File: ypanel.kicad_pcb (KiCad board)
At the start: 6 copper layers, 64 x 58 mm, 58 parts, among them IC2 TSL2561, J1 XF2M-1015-1A, J2 Conn_Coaxial, J3 BATTERY CONNECTOR, J4 B2B-PH-SM4-TB_LF__SN_, U2 Value, U3 SW_SPDT, U4 SW_SPDT

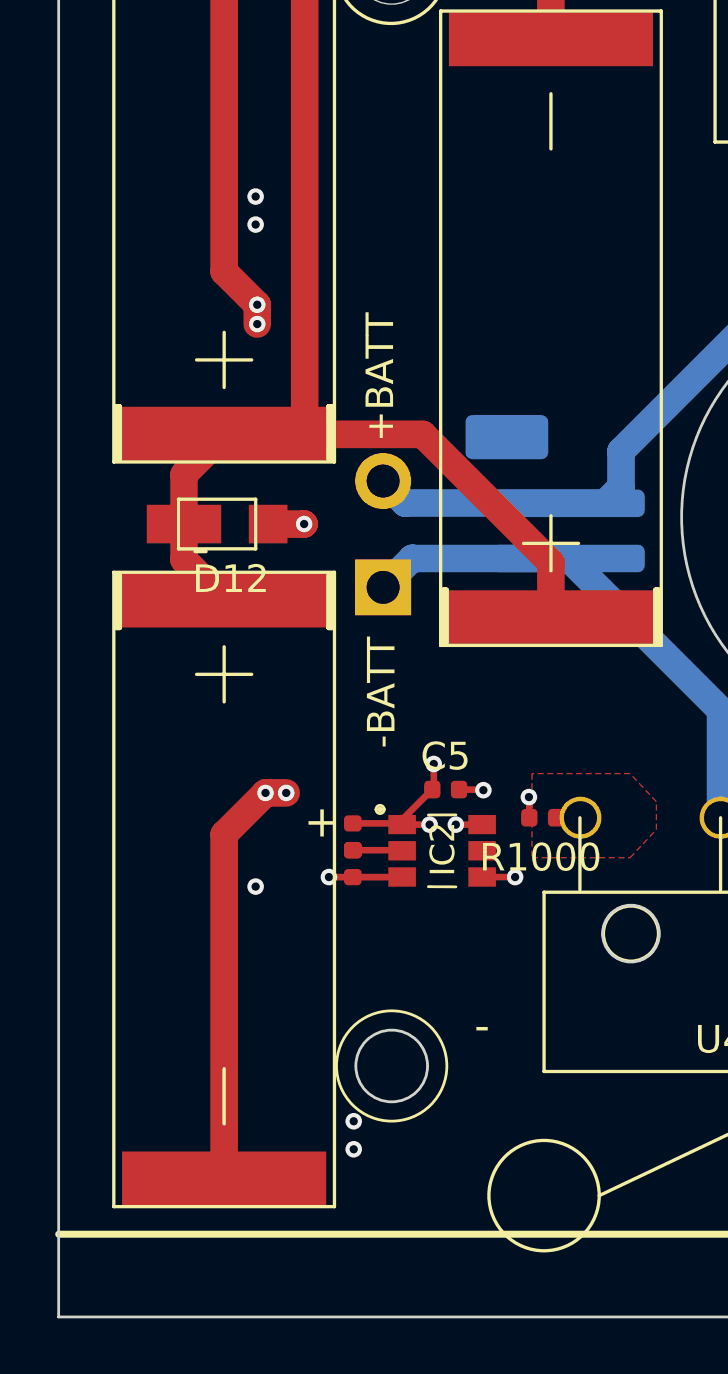
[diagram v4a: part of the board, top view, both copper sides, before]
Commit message: Changed magnetorquer coils
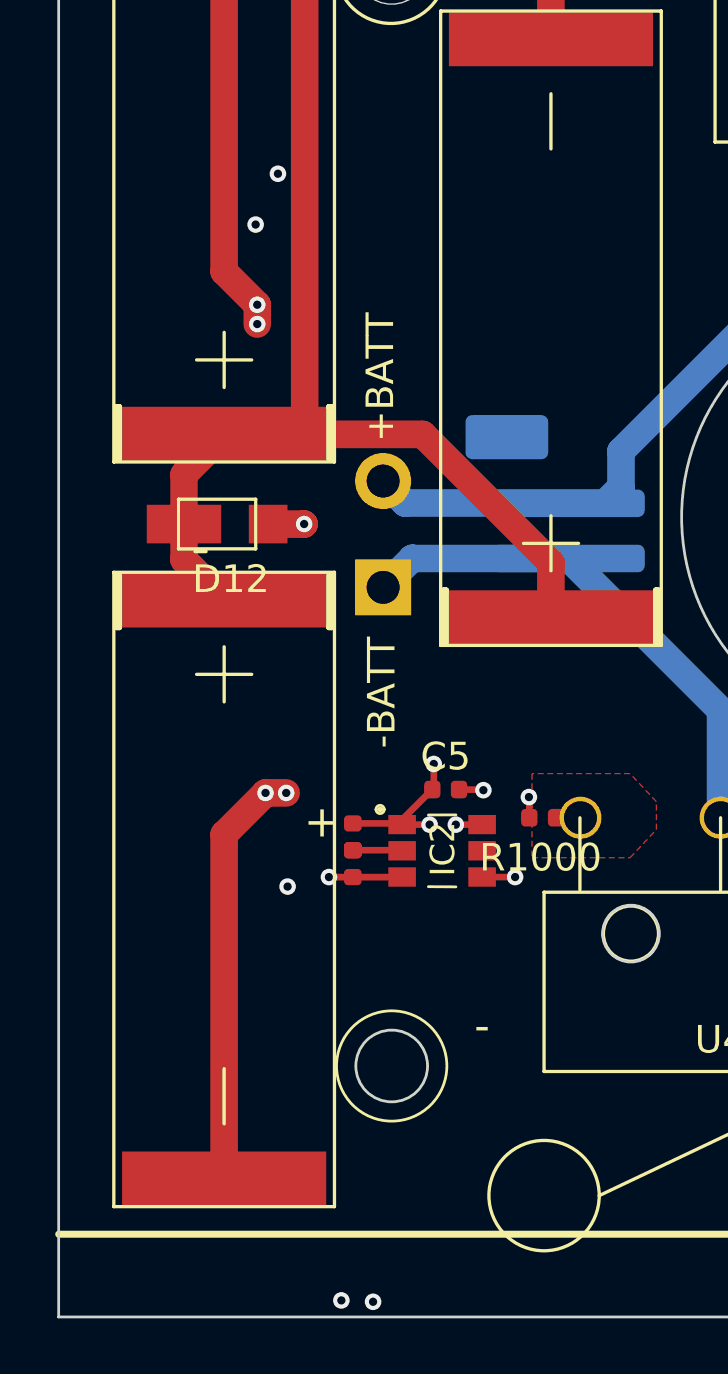
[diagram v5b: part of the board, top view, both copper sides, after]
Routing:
- net /coil: track 15890.0 -> 16804.3 mm
- net COIL_N: track 50.9 -> 43.0 mm
- net BATT_N: track 34.9 -> 30.4 mm
- net COIL_P: track 50.3 -> 45.8 mm
- net BATT_P: track 62.1 -> 58.9 mm

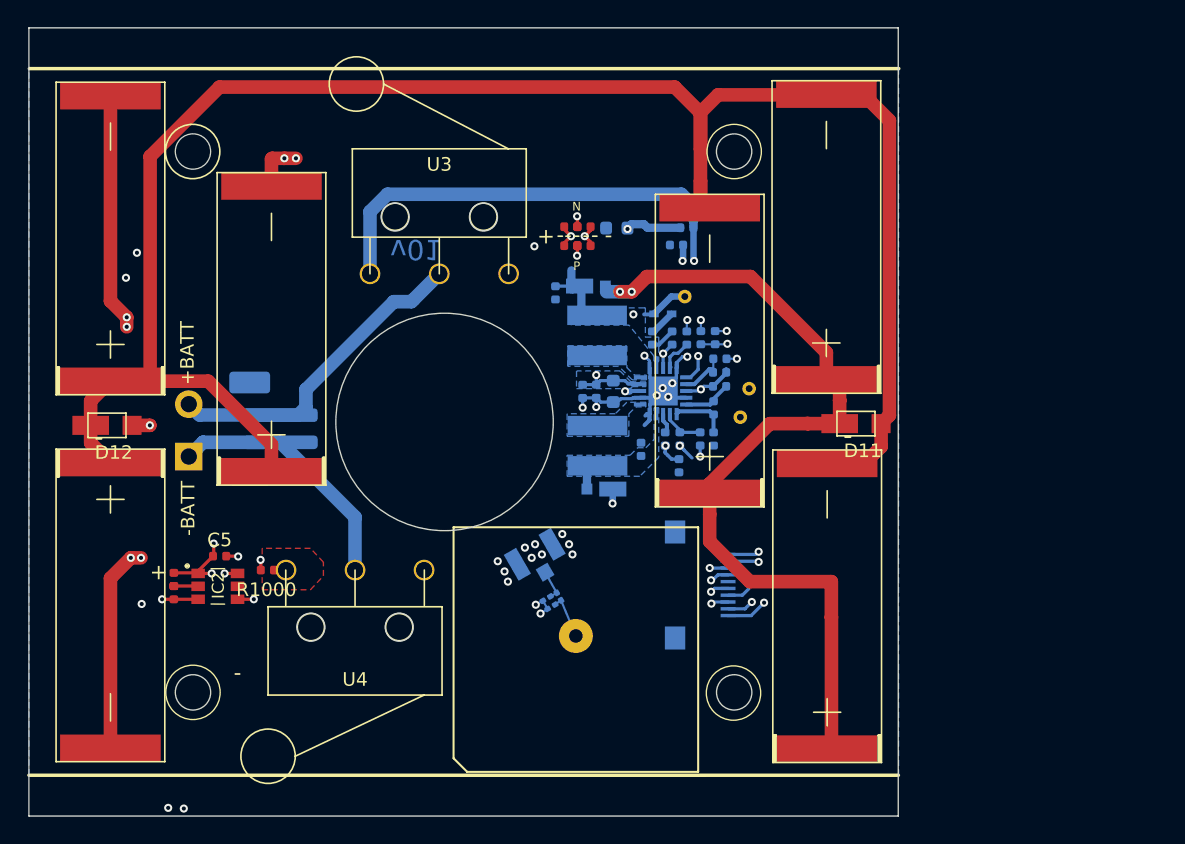
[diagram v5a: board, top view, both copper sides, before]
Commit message: added fiducials, regenerated 3d model and gerbers
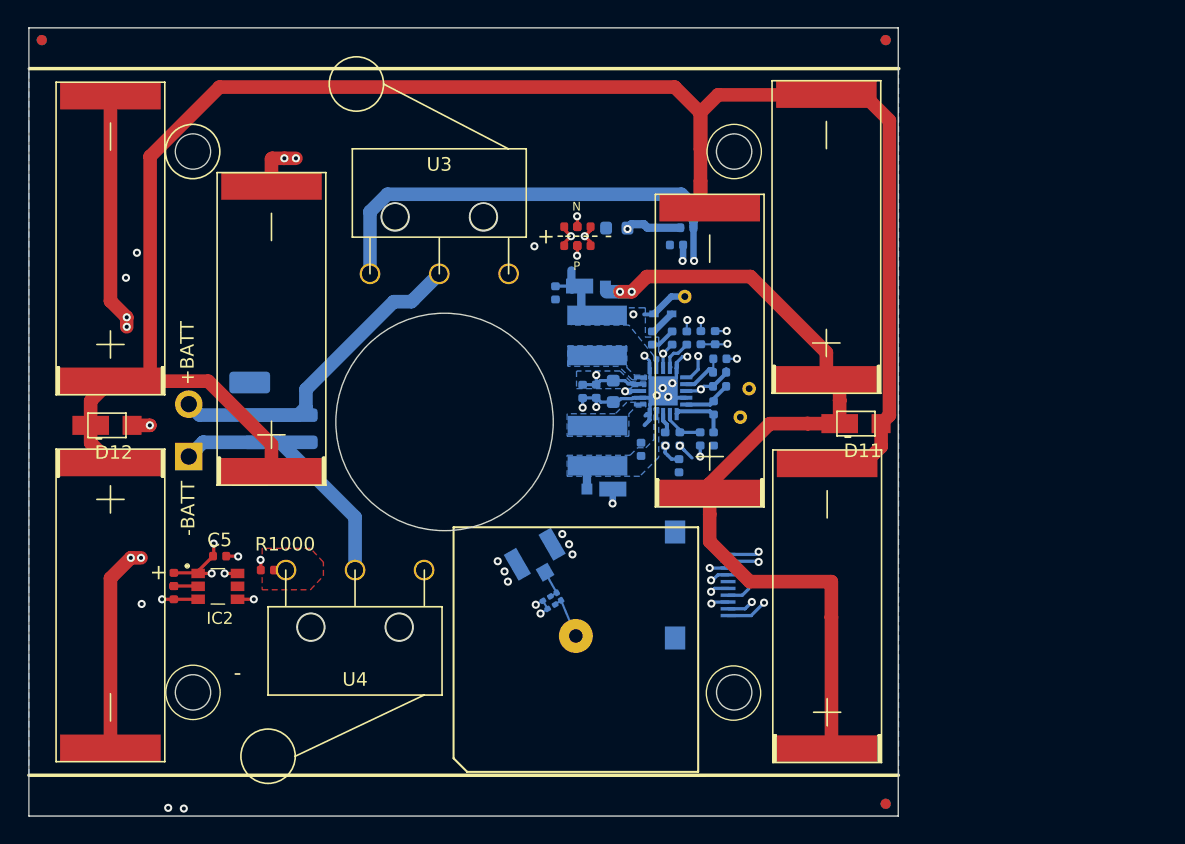
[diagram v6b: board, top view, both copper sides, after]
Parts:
- added REF**: Fiducial_0.75mm_Mask1.5mm, Fiducial:Fiducial_0.75mm_Mask1.5mm, B.Cu at (114.0, 70.9)
- added REF**: Fiducial_0.75mm_Mask1.5mm, Fiducial:Fiducial_0.75mm_Mask1.5mm, B.Cu at (176.1, 70.9)
- added REF**: Fiducial_0.75mm_Mask1.5mm, Fiducial:Fiducial_0.75mm_Mask1.5mm, B.Cu at (176.1, 127.1)
- added REF**: Fiducial_0.75mm_Mask1.5mm, Fiducial:Fiducial_0.75mm_Mask1.5mm, F.Cu at (176.1, 127.1)
- added REF**: Fiducial_0.75mm_Mask1.5mm, Fiducial:Fiducial_0.75mm_Mask1.5mm, F.Cu at (176.1, 70.9)
- added REF**: Fiducial_0.75mm_Mask1.5mm, Fiducial:Fiducial_0.75mm_Mask1.5mm, F.Cu at (114.0, 70.9)
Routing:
- net COIL_P: track 45.8 -> 48.3 mm
- net COIL_N: track 43.0 -> 44.2 mm
- net GND: vias 36 -> 32
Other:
- rule pad_to_mask_clearance: 0.0508 -> 0.049
- rule solder_mask_min_width: 0.25 -> 0.099
- board text added: "v02"

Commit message: clean up & manufacturing output for v3
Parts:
- removed C12, C13: TBD, Capacitor_SMD:C_0201_0603Metric
- removed L3: TBD, Inductor_SMD:L_0201_0603Metric
- moved TP2 36.1 mm to (130.9, 88.1)
- moved REF** 7.15 mm to (174.5, 120.1) (x2)
- moved REF** 7.15 mm to (116.7, 77.5) (x2)
- moved REF** 6.93 mm to (174.0, 77.5) (x2)
- moved R1000 1.70 mm to (130.6, 108.2), turned to 90 degrees
- moved C1 1.33 mm to (159.8, 103.0)
- moved J2 1.00 mm to (149.5, 109.5), turned to 125 degrees
- moved TP1 0.97 mm to (165.0, 99.6)
- moved R5 0.33 mm to (163.4, 98.3)
- moved R8 0.28 mm to (162.1, 100.2)
- moved R12 0.20 mm to (163.7, 92.8)
- moved D2 0.16 mm to (155.3, 104.1)
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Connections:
- IC2 pad 5: (no net) -> Net-(IC2-Pad5)
- J1 pad 5: (no net) -> BURN1
- J2 pad 1: Net-(C12-Pad1) -> Net-(AE1-Pad1)
- U3 pad 1: (no net) -> Net-(U3-Pad1)
- U4 pad 1: (no net) -> Net-(U4-Pad1)
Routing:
- net GND: track 68.8 -> 65.4 mm, vias 32 -> 31
- net Net-(C12-Pad1): track 2.27 -> 0.00 mm
- net Net-(AE1-Pad1): track 3.37 -> 5.39 mm
- net /VSOLAR_FULL: track 65.6 -> 67.1 mm
- net VOUT_EN: track 11.4 -> 10.1 mm
- net +3V3: track 65.1 -> 63.8 mm, vias 4 -> 3
- net Net-(D11-Pad2): track 136.4 -> 135.2 mm
- net Net-(J3-Pad1): track 18.9 -> 19.6 mm
- net Net-(R7-Pad2): track 3.80 -> 3.23 mm
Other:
- board text added: "JLCJLCJLCJLC"
- board text removed: "Cable Pinout 1.BATT_P 2.BATT_N 3.SDA 4.SCL 5.BURN 6.3V3 7.GND 8.GND 9.COIL_N 10.COIL_P"
- board text removed: "coil_n"
- board text removed: "coil_p"
- board text removed: "v01"

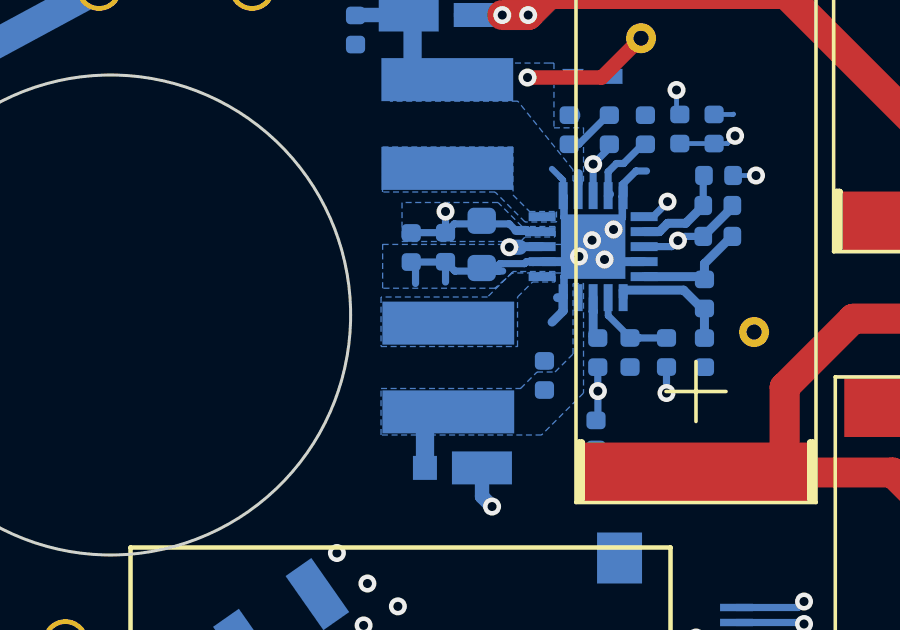
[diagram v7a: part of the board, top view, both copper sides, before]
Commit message: should actually be v3
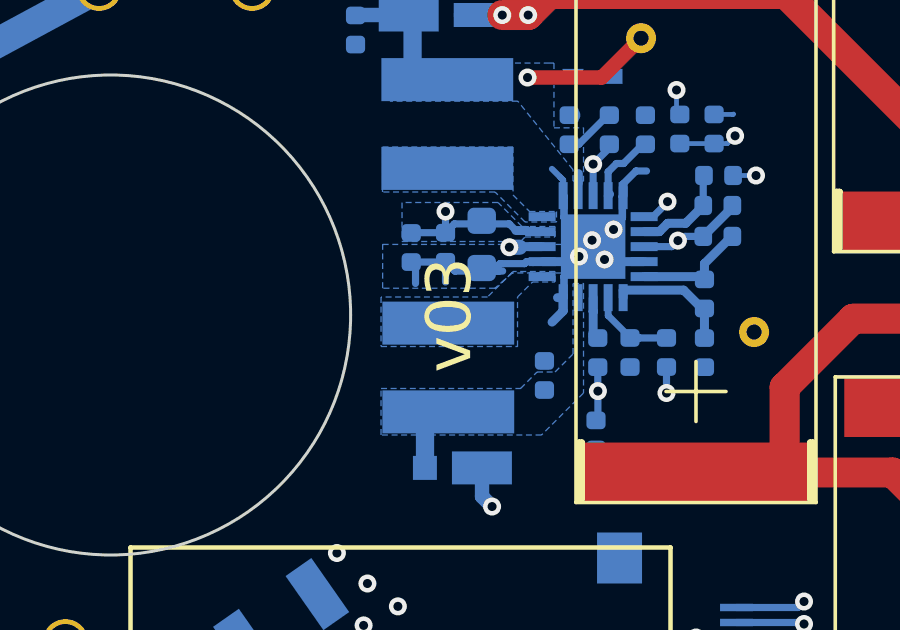
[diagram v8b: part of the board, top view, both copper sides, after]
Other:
- board text added: "v03"
- board text removed: "v02"
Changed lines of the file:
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@@
   (general
     (thickness 1.6)
-    (drawings 107)
+    (drawings 108)
     (tracks 1136)
     (zones 0)
@@
     (35 F.Paste user hide)
     (36 B.SilkS user)
-    (37 F.SilkS user)
+    (37 F.SilkS user hide)
     (38 B.Mask user hide)
     (39 F.Mask user hide)
@@
       (solder_mask_margin 0.375) (clearance 0.375))
   )
+  (gr_text v03 (at 154.8765 99.000001 90) (layer F.SilkS)
+    (effects (font (size 1.5 1.5) (thickness 0.3)))
+  )
   (gr_text JLCJLCJLCJLC (at 171.704 85.344 90) (layer F.SilkS)
     (effects (font (size 0.9 0.9) (thickness 0.15)))
@@
   (gr_line (start 121.6 75.6) (end 168.4 75.6) (layer Dwgs.User) (width 0.15))
   (gr_circle (center 164.895 79.10248) (end 166.195 79.10248) (layer Edge.Cuts) (width 0.1))
-  (gr_text v02 (at 155.2 79.3) (layer B.SilkS)
+  (gr_text v03 (at 155.2 79.3) (layer B.SilkS)
     (effects (font (size 1.5 1.5) (thickness 0.3)) (justify mirror))
   )
